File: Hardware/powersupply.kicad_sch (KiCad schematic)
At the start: 30 parts, among them J4 USB_C_Receptacle_USB2.0_16P, J8 Conn_01x02_Pin, Q1 Dual_NMOS_8205A, U2 AMS1117-3.3, U3 DW01A, U6 TP4056, U9 XC6220B181MR

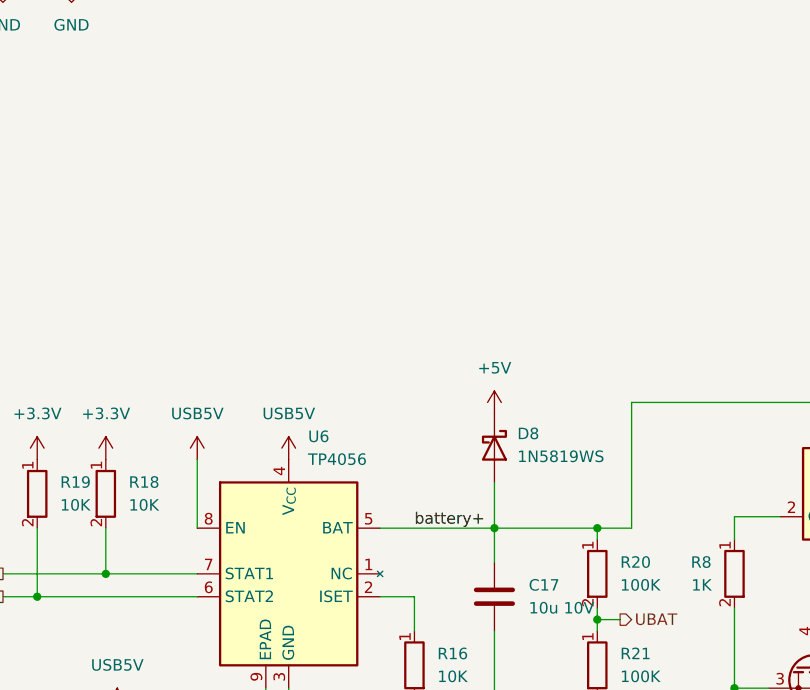
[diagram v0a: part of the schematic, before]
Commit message: wip
added screenshots, modified battery connection and silkscreen
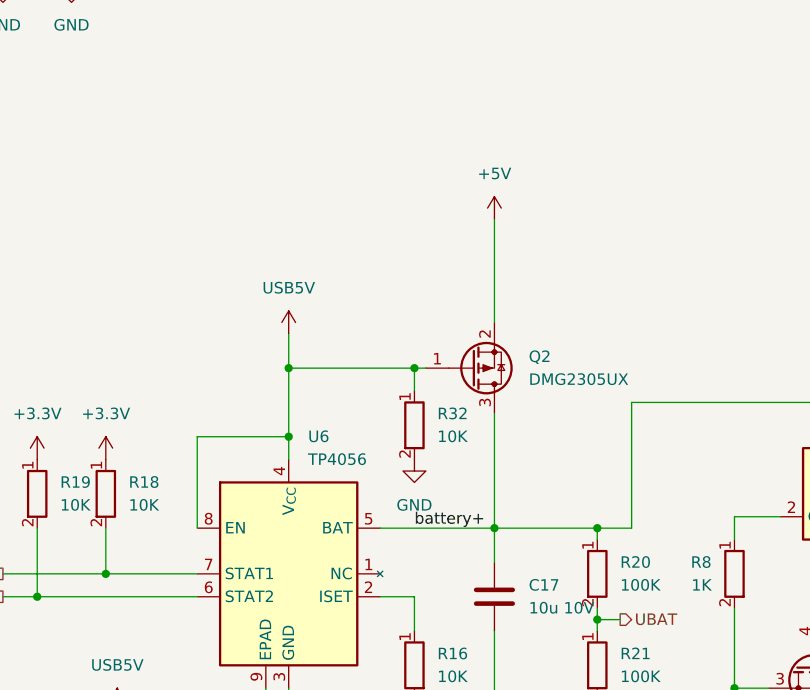
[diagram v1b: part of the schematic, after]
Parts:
- removed D8: 1N5819WS, Diode_SMD:D_SOD-323, symbol Diode:1N5819WS
- added Q2: DMG2305UX, Package_TO_SOT_SMD:SOT-23-3, symbol Transistor_FET:Q_PMOS_GSD
- added R32: 10K, Resistor_SMD:R_0603_1608Metric, symbol Resistor_E12_0603:Resistor 10K
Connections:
- net +5V: now also Q2.2 (S)
- net GND: now also R32.2
- net USB5V: now also Q2.1 (G), R32.1
- net battery+: now also Q2.3 (D)

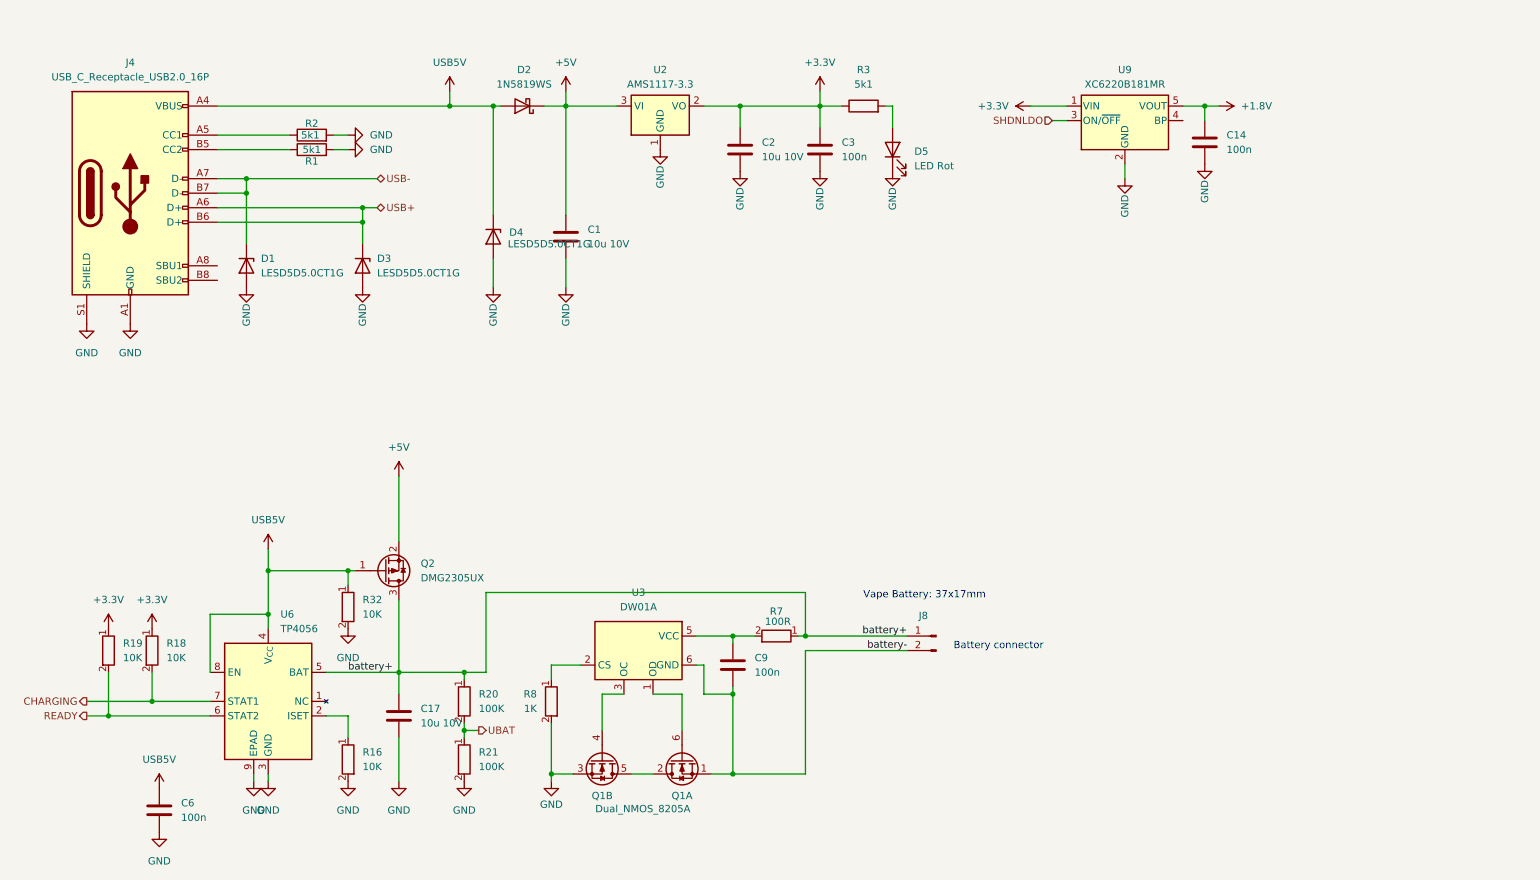
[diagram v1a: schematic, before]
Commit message: First Release
HW ordered at Aisler, SW wip
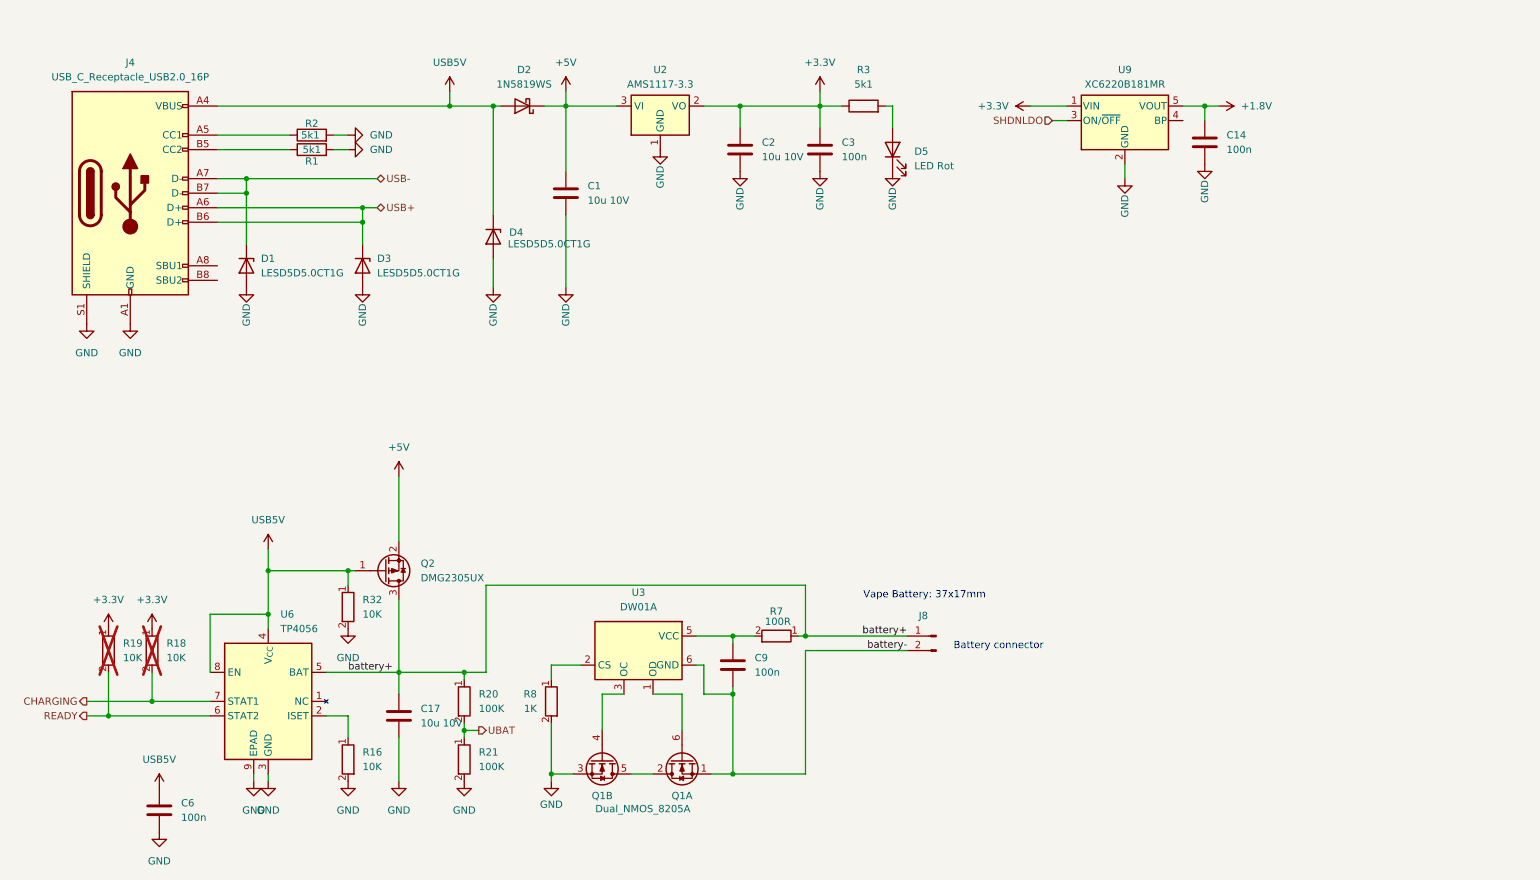
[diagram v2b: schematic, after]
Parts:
- R18, R19: now not fitted
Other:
- moved on the sheet: C1
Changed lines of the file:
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@@
 	(wire
 		(pts
-			(xy 115.57 69.85) (xy 115.57 64.77)
+			(xy 115.57 69.85) (xy 115.57 57.15)
 		)
 		(stroke
@@
 	(wire
 		(pts
-			(xy 115.57 38.1) (xy 115.57 57.15)
+			(xy 115.57 38.1) (xy 115.57 49.53)
 		)
 		(stroke
@@
 	(wire
 		(pts
-			(xy 101.6 137.16) (xy 101.6 123.19)
+			(xy 101.6 137.16) (xy 101.6 121.92)
 		)
 		(stroke
@@
 	(wire
 		(pts
-			(xy 157.48 123.19) (xy 157.48 130.81)
+			(xy 157.48 121.92) (xy 157.48 130.81)
 		)
 		(stroke
@@
 	(wire
 		(pts
-			(xy 101.6 123.19) (xy 157.48 123.19)
+			(xy 101.6 121.92) (xy 157.48 121.92)
 		)
 		(stroke
@@
 		(in_bom yes)
 		(on_board yes)
-		(dnp no)
+		(dnp yes)
 		(fields_autoplaced yes)
 		(property "Reference" "R19"
@@
 		(in_bom yes)
 		(on_board yes)
-		(dnp no)
+		(dnp yes)
 		(fields_autoplaced yes)
 		(property "Reference" "R18"
@@
 	(symbol
 		(lib_id "_PS_LIB:C_0603")
-		(at 115.57 60.96 0)
+		(at 115.57 53.34 0)
 		(unit 1)
 		(exclude_from_sim no)
@@
 		(fields_autoplaced yes)
 		(property "Reference" "C1"
-			(at 119.38 59.6899 0)
+			(at 119.38 52.0699 0)
 			(effects
 				(font
@@
 		)
 		(property "Value" "10u 10V"
-			(at 119.38 62.2299 0)
+			(at 119.38 54.6099 0)
 			(effects
 				(font
@@
 		)
 		(property "Footprint" "Capacitor_SMD:C_0603_1608Metric"
-			(at 116.5352 64.77 0)
+			(at 116.5352 57.15 0)
 			(effects
 				(font
@@
 		)
 		(property "Datasheet" "~"
-			(at 115.57 60.96 0)
+			(at 115.57 53.34 0)
 			(effects
 				(font
@@
 		)
 		(property "Description" "Unpolarized capacitor"
-			(at 115.57 60.96 0)
+			(at 115.57 53.34 0)
 			(effects
 				(font
@@
 		)
 		(property "Characteristics" ""
-			(at 115.57 60.96 0)
+			(at 115.57 53.34 0)
 			(effects
 				(font
@@
 		)
 		(property "LCSC" "C2959727"
-			(at 115.57 60.96 0)
+			(at 115.57 53.34 0)
 			(effects
 				(font

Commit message: adding buck-boost
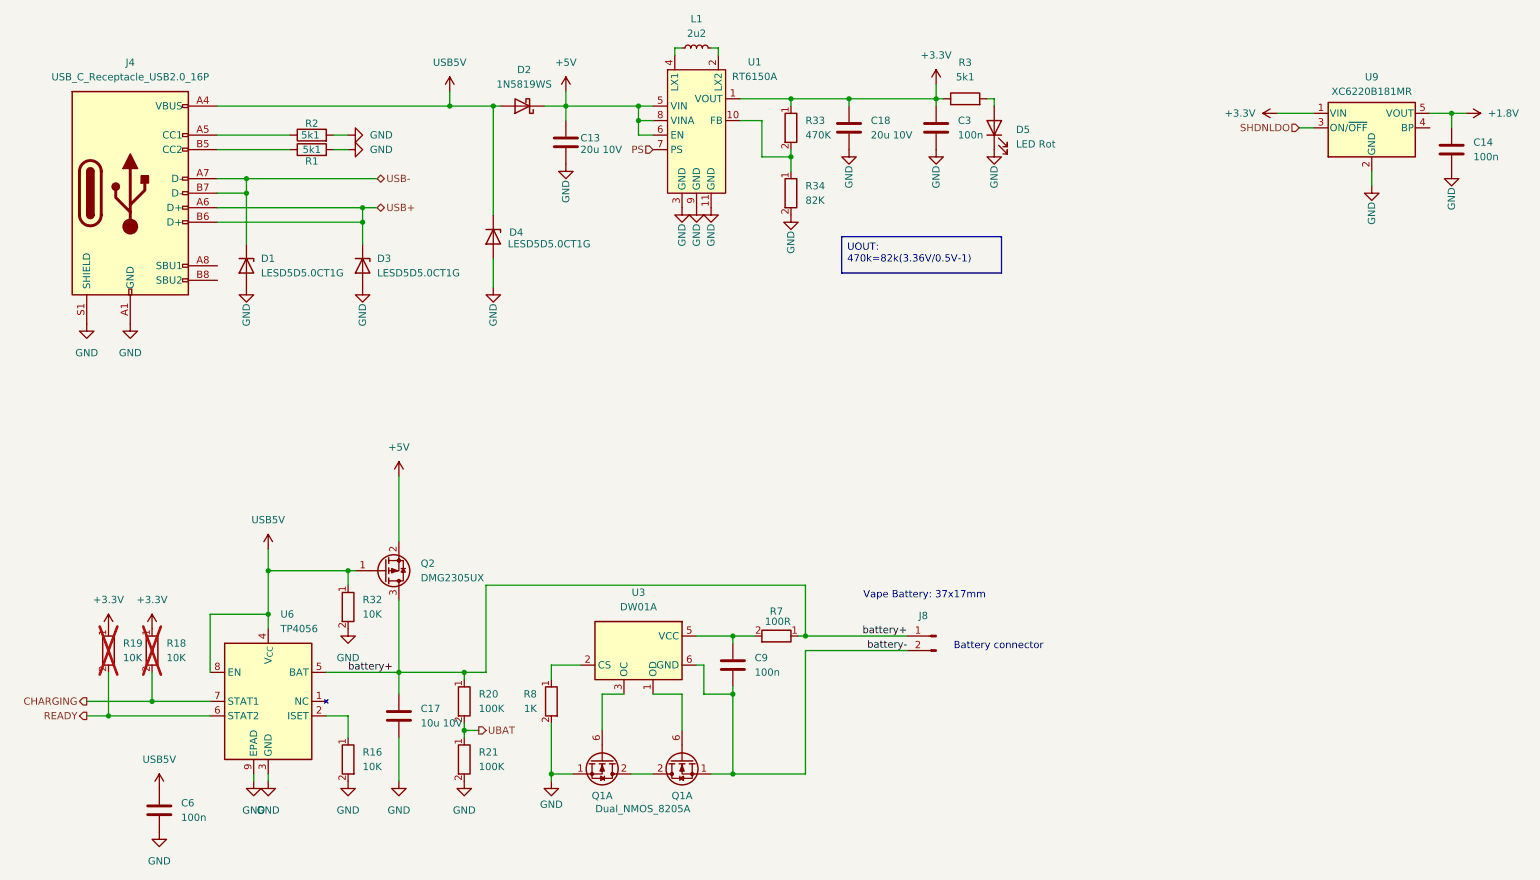
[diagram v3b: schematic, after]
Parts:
- removed C1, C2: 10u 10V, Capacitor_SMD:C_0603_1608Metric, symbol _PS_LIB:C_0603
- removed U2: AMS1117-3.3, Package_TO_SOT_SMD:SOT-223-3_TabPin2, symbol Regulator_Linear:AMS1117-3.3
- added C13, C18: 20u 10V, Capacitor_SMD:C_0805_2012Metric, symbol _PS_LIB:C_1206
- added L1: 2u2, Inductor_SMD:L_0603_1608Metric, symbol Device:L_Small
- added R33: 470K, Resistor_SMD:R_0603_1608Metric, symbol Resistor_E12_0603:Resistor 470K
- added R34: 82K, Resistor_SMD:R_0603_1608Metric, symbol Resistor_E12_0603:Resistor 82K
- added U1: RT6150A, Package_DFN_QFN:WDFN-10-1EP_3x3mm_P0.5mm_EP1.8x2.5mm, symbol PS_IC:RT6150A
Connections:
- net +3.3V: now also C18.1, R33.1, U1.1 (VOUT)
- net +5V: now also C13.1, U1.5 (VIN), U1.6 (EN), U1.8 (VINA)
- net GND: now also Q1.1 (S), C13.2, C18.2, R34.2, U1.11 (GND), U1.3 (GND), U1.9 (GND); no longer Q1.3 (S)
- net at U3.3 (OC): now also Q1.6 (G); no longer Q1.4 (G)
- net at Q1.2 (D): now also Q1.2 (D); no longer Q1.5 (D)
- new net: R33.2, R34.1, U1.10 (FB)
- new net: L1.1, U1.4 (LX1)
- new net: L1.2, U1.2 (LX2)
- new net PS: U1.7 (PS)
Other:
- moved on the sheet: C14, C3, D5, R3, U9

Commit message: wip
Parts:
- renumbered U1 to U2
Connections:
- net GND: now also Q1.3 (S); no longer Q1.1 (S)
- net at Q1.2 (D): now also Q1.5 (D); no longer Q1.2 (D)
- net at U3.3 (OC): now also Q1.4 (G); no longer Q1.6 (G)

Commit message: mqtt und oled implementiert wip
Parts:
- removed R16: 10K, Resistor_SMD:R_0603_1608Metric, symbol Resistor_E12_0603:Resistor 10K
- added R16: 3K9, Resistor_SMD:R_0603_1608Metric, symbol Resistor_E12_0603:Resistor 3K9
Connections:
- net GND: now also R16.2
- net at U6.2 (ISET): now also R16.1

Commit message: V2 fertig gestellt!
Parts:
- removed R18, R19: 10K, Resistor_SMD:R_0603_1608Metric, symbol Resistor_E12_0603:Resistor 10K
- J8: footprint Connector_PinHeader_2.00mm:PinHeader_1x02_P2.00mm_Vertical -> Connector_JST:JST_PH_B2B-PH-K_1x02_P2.00mm_Vertical
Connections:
- net battery+: now also J8.2 (Pin_2); no longer J8.1 (Pin_1)
- net battery-: now also J8.1 (Pin_1); no longer J8.2 (Pin_2)
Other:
- note removed: "Vape Battery: 37x17mm"
- moved on the sheet: J8

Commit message: housing created
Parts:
- removed C14: 100n, Capacitor_SMD:C_0603_1608Metric, symbol _PS_LIB:C_0603
- removed U9: XC6220B181MR, Package_TO_SOT_SMD:SOT-23-5, symbol Regulator_Linear:LP2985-1.8

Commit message: license
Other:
- company: (none) -> hand-crafted-electronics
- title: (none) -> Power Supply
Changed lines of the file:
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@@
 	(generator_version "9.0")
 	(paper "A4")
+	(title_block
+		(title "Power Supply")
+		(date "2026-01-09")
+		(rev "2")
+		(company "hand-crafted-electronics")
+		(comment 1 "https://ohwr.org/cern_ohl_s_v2.txt")
+		(comment 2 "https://github.com/pellematrose/ESP32-C3_Sensor/")
+		(comment 3 "Licensed under CERN-OHL-S v2")
+		(comment 4 "2026 Per-Simon Saal")
+	)
 	(text "Battery connector"
 		(exclude_from_sim no)
